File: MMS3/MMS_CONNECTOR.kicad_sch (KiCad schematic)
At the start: 6 parts, among them J8 RJ45_LED_Shielded, U4 TPD2EUSB30DRTR-TP

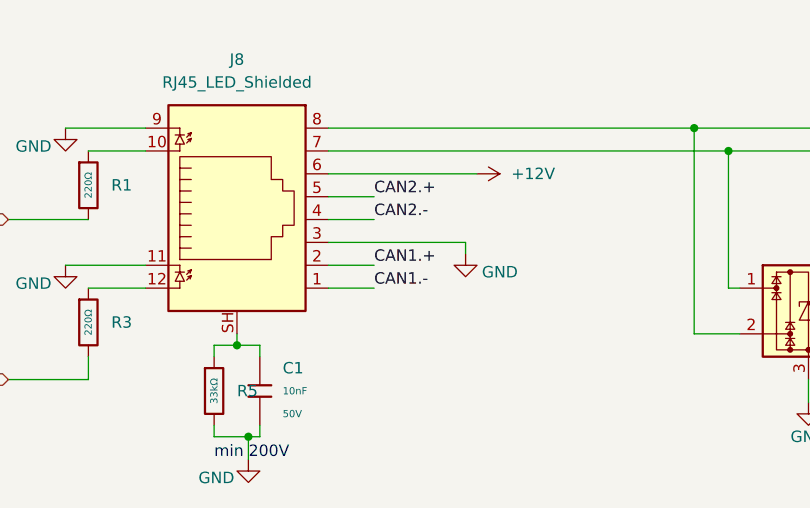
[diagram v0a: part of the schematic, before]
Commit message: schematic + partly layout
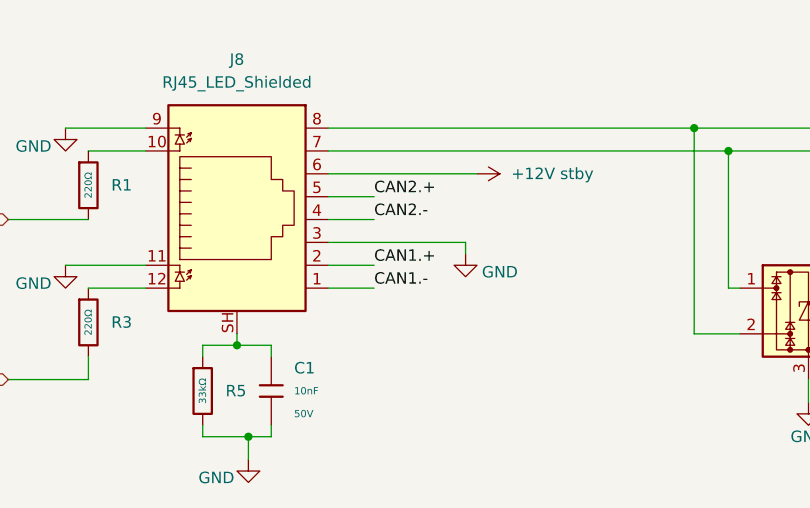
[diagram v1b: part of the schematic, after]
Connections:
- net +12V renamed +12V stby
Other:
- note removed: "min 200V"
- moved on the sheet: C1, R5
